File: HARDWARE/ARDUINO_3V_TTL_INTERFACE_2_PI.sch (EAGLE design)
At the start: 41 parts, among them J1 RASPBERRYPI-40-PIN-GPIO_SMT, Q1 BCM857BS, Q2 DMG2305UX, U1 ATMEGA328P, Y1 8MHz

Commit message: checkiong migration to new profile
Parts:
- D1: value GREEN -> RED
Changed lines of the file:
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@@
 <grid distance="0.1" unitdist="inch" unit="inch" style="lines" multiple="1" display="no" altdistance="0.01" altunitdist="inch" altunit="inch"/>
 <layers>
-<layer number="1" name="Top" color="4" fill="1" visible="yes" active="no"/>
-<layer number="2" name="Route2" color="16" fill="1" visible="yes" active="no"/>
-<layer number="3" name="Route3" color="17" fill="1" visible="yes" active="no"/>
-<layer number="4" name="Route4" color="18" fill="1" visible="yes" active="no"/>
-<layer number="5" name="Route5" color="19" fill="1" visible="yes" active="no"/>
-<layer number="6" name="Route6" color="25" fill="1" visible="yes" active="no"/>
-<layer number="7" name="Route7" color="26" fill="1" visible="yes" active="no"/>
-<layer number="8" name="Route8" color="27" fill="1" visible="yes" active="no"/>
-<layer number="9" name="Route9" color="28" fill="1" visible="yes" active="no"/>
-<layer number="10" name="Route10" color="29" fill="1" visible="yes" active="no"/>
-<layer number="11" name="Route11" color="30" fill="1" visible="yes" active="no"/>
-<layer number="12" name="Route12" color="20" fill="1" visible="yes" active="no"/>
-<layer number="13" name="Route13" color="21" fill="1" visible="yes" active="no"/>
-<layer number="14" name="Route14" color="22" fill="1" visible="yes" active="no"/>
-<layer number="15" name="Route15" color="23" fill="1" visible="yes" active="no"/>
-<layer number="16" name="Bottom" color="1" fill="1" visible="yes" active="no"/>
-<layer number="17" name="Pads" color="2" fill="1" visible="yes" active="no"/>
-<layer number="18" name="Vias" color="2" fill="1" visible="yes" active="no"/>
-<layer number="19" name="Unrouted" color="6" fill="1" visible="yes" active="no"/>
-<layer number="20" name="Dimension" color="24" fill="1" visible="yes" active="no"/>
-<layer number="21" name="tPlace" color="7" fill="1" visible="yes" active="no"/>
-<layer number="22" name="bPlace" color="7" fill="1" visible="yes" active="no"/>
-<layer number="23" name="tOrigins" color="15" fill="1" visible="yes" active="no"/>
-<layer number="24" name="bOrigins" color="15" fill="1" visible="yes" active="no"/>
-<layer number="25" name="tNames" color="7" fill="1" visible="yes" active="no"/>
-<layer number="26" name="bNames" color="7" fill="1" visible="yes" active="no"/>
-<layer number="27" name="tValues" color="7" fill="1" visible="yes" active="no"/>
-<layer number="28" name="bValues" color="7" fill="1" visible="yes" active="no"/>
+<layer number="1" name="Top" color="4" fill="1" visible="no" active="no"/>
+<layer number="2" name="Route2" color="16" fill="1" visible="no" active="no"/>
+<layer number="3" name="Route3" color="17" fill="1" visible="no" active="no"/>
+<layer number="4" name="Route4" color="18" fill="1" visible="no" active="no"/>
+<layer number="5" name="Route5" color="19" fill="1" visible="no" active="no"/>
+<layer number="6" name="Route6" color="25" fill="1" visible="no" active="no"/>
+<layer number="7" name="Route7" color="26" fill="1" visible="no" active="no"/>
+<layer number="8" name="Route8" color="27" fill="1" visible="no" active="no"/>
+<layer number="9" name="Route9" color="28" fill="1" visible="no" active="no"/>
+<layer number="10" name="Route10" color="29" fill="1" visible="no" active="no"/>
+<layer number="11" name="Route11" color="30" fill="1" visible="no" active="no"/>
+<layer number="12" name="Route12" color="20" fill="1" visible="no" active="no"/>
+<layer number="13" name="Route13" color="21" fill="1" visible="no" active="no"/>
+<layer number="14" name="Route14" color="22" fill="1" visible="no" active="no"/>
+<layer number="15" name="Route15" color="23" fill="1" visible="no" active="no"/>
+<layer number="16" name="Bottom" color="1" fill="1" visible="no" active="no"/>
+<layer number="17" name="Pads" color="2" fill="1" visible="no" active="no"/>
+<layer number="18" name="Vias" color="2" fill="1" visible="no" active="no"/>
+<layer number="19" name="Unrouted" color="6" fill="1" visible="no" active="no"/>
+<layer number="20" name="Dimension" color="24" fill="1" visible="no" active="no"/>
+<layer number="21" name="tPlace" color="7" fill="1" visible="no" active="no"/>
+<layer number="22" name="bPlace" color="7" fill="1" visible="no" active="no"/>
+<layer number="23" name="tOrigins" color="15" fill="1" visible="no" active="no"/>
+<layer number="24" name="bOrigins" color="15" fill="1" visible="no" active="no"/>
+<layer number="25" name="tNames" color="7" fill="1" visible="no" active="no"/>
+<layer number="26" name="bNames" color="7" fill="1" visible="no" active="no"/>
+<layer number="27" name="tValues" color="7" fill="1" visible="no" active="no"/>
+<layer number="28" name="bValues" color="7" fill="1" visible="no" active="no"/>
 <layer number="29" name="tStop" color="7" fill="3" visible="no" active="no"/>
 <layer number="30" name="bStop" color="7" fill="6" visible="no" active="no"/>
@@
 <layer number="35" name="tGlue" color="7" fill="4" visible="no" active="no"/>
 <layer number="36" name="bGlue" color="7" fill="5" visible="no" active="no"/>
-<layer number="37" name="tTest" color="7" fill="1" visible="yes" active="no"/>
-<layer number="38" name="bTest" color="7" fill="1" visible="yes" active="no"/>
+<layer number="37" name="tTest" color="7" fill="1" visible="no" active="no"/>
+<layer number="38" name="bTest" color="7" fill="1" visible="no" active="no"/>
 <layer number="39" name="tKeepout" color="4" fill="11" visible="no" active="no"/>
 <layer number="40" name="bKeepout" color="1" fill="11" visible="no" active="no"/>
@@
 <layer number="44" name="Drills" color="7" fill="1" visible="no" active="no"/>
 <layer number="45" name="Holes" color="7" fill="1" visible="no" active="no"/>
-<layer number="46" name="Milling" color="3" fill="1" visible="yes" active="no"/>
-<layer number="47" name="Measures" color="7" fill="1" visible="yes" active="no"/>
-<layer number="48" name="Document" color="7" fill="1" visible="yes" active="no"/>
-<layer number="49" name="Reference" color="7" fill="1" visible="yes" active="no"/>
-<layer number="50" name="dxf" color="7" fill="1" visible="yes" active="no"/>
-<layer number="51" name="tDocu" color="7" fill="1" visible="yes" active="no"/>
-<layer number="52" name="bDocu" color="7" fill="1" visible="yes" active="no"/>
-<layer number="53" name="tGND_GNDA" color="7" fill="9" visible="yes" active="no"/>
-<layer number="54" name="bGND_GNDA" color="1" fill="9" visible="yes" active="no"/>
-<layer number="56" name="wert" color="7" fill="1" visible="yes" active="no"/>
-<layer number="57" name="tCAD" color="7" fill="1" visible="yes" active="no"/>
-<layer number="59" name="tCarbon" color="7" fill="1" visible="yes" active="no"/>
-<layer number="60" name="bCarbon" color="7" fill="1" visible="yes" active="no"/>
+<layer number="46" name="Milling" color="3" fill="1" visible="no" active="no"/>
+<layer number="47" name="Measures" color="7" fill="1" visible="no" active="no"/>
+<layer number="48" name="Document" color="7" fill="1" visible="no" active="no"/>
+<layer number="49" name="Reference" color="7" fill="1" visible="no" active="no"/>
+<layer number="50" name="dxf" color="7" fill="1" visible="no" active="no"/>
+<layer number="51" name="tDocu" color="7" fill="1" visible="no" active="no"/>
+<layer number="52" name="bDocu" color="7" fill="1" visible="no" active="no"/>
+<layer number="53" name="tGND_GNDA" color="7" fill="9" visible="no" active="no"/>
+<layer number="54" name="bGND_GNDA" color="1" fill="9" visible="no" active="no"/>
+<layer number="56" name="wert" color="7" fill="1" visible="no" active="no"/>
+<layer number="57" name="tCAD" color="7" fill="1" visible="no" active="no"/>
+<layer number="59" name="tCarbon" color="7" fill="1" visible="no" active="no"/>
+<layer number="60" name="bCarbon" color="7" fill="1" visible="no" active="no"/>
 <layer number="88" name="SimResults" color="9" fill="1" visible="yes" active="yes"/>
 <layer number="89" name="SimProbes" color="9" fill="1" visible="yes" active="yes"/>
@@
 <part name="GND3" library="3-5-pin-smd" library_urn="urn:adsk.eagle:library:7170558" deviceset="GND" device=""/>
 <part name="C4" library="SparkFun-Capacitors" library_urn="urn:adsk.eagle:library:510" deviceset="0.1UF" device="-0603-100V-10%" package3d_urn="urn:adsk.eagle:package:37414/1" value="0.1uF"/>
-<part name="D1" library="SparkFun-LED" library_urn="urn:adsk.eagle:library:529" deviceset="LED-GREEN" device="0603" package3d_urn="urn:adsk.eagle:package:39354/1" value="GREEN"/>
+<part name="D1" library="SparkFun-LED" library_urn="urn:adsk.eagle:library:529" deviceset="LED-GREEN" device="0603" package3d_urn="urn:adsk.eagle:package:39354/1" value="RED"/>
 <part name="R2" library="SparkFun-Resistors" library_urn="urn:adsk.eagle:library:532" deviceset="10KOHM" device="-0603-1/10W-1%" package3d_urn="urn:adsk.eagle:package:39650/1" value="330"/>
 <part name="GND4" library="3-5-pin-smd" library_urn="urn:adsk.eagle:library:7170558" deviceset="GND" device=""/>

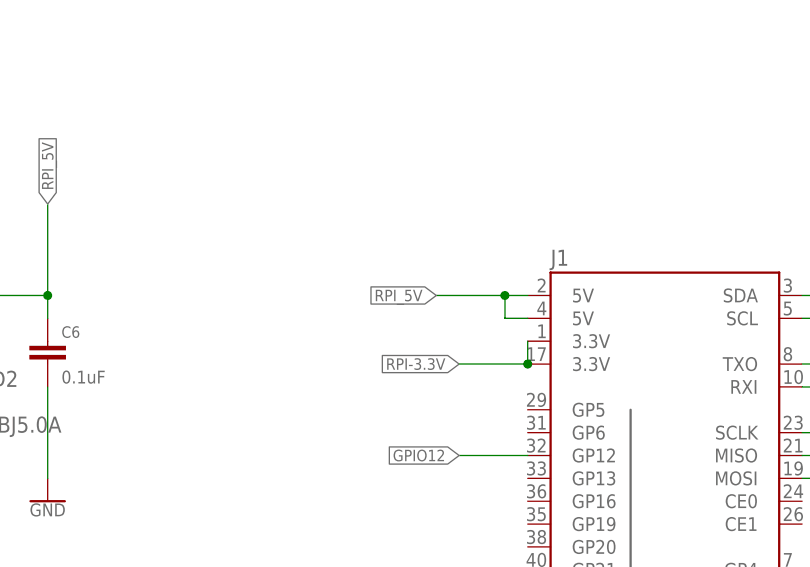
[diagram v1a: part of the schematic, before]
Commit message: added a jumper to separate ext voltage for testing it the volt reg citcuit doesn't work
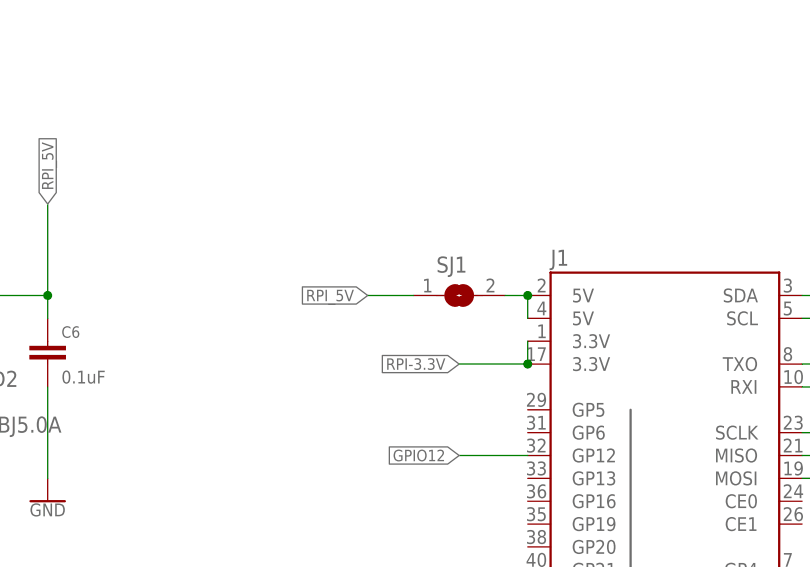
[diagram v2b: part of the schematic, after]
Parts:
- added SJ1: (no value), jumper:SJ
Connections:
- new net N$2: J1.5V@2, J1.5V@4, SJ1.2
- net RPI_5V: now also SJ1.1; no longer J1.5V@2, J1.5V@4
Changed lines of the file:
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@@
 <part name="GND5" library="3-5-pin-smd" library_urn="urn:adsk.eagle:library:7170558" deviceset="GND" device=""/>
 <part name="J13" library="SparkFun-Connectors" library_urn="urn:adsk.eagle:library:513" deviceset="CONN_09" device="" package3d_urn="urn:adsk.eagle:package:38153/1"/>
+<part name="SJ1" library="jumper" library_urn="urn:adsk.eagle:library:252" deviceset="SJ" device="" package3d_urn="urn:adsk.eagle:package:15471/1"/>
 </parts>
 <sheets>
@@
 <attribute name="VALUE" x="127" y="12.954" size="1.778" layer="96" font="vector"/>
 <attribute name="NAME" x="127" y="41.148" size="1.778" layer="95" font="vector"/>
+</instance>
+<instance part="SJ1" gate="1" x="45.72" y="68.58" smashed="yes">
+<attribute name="NAME" x="43.18" y="71.12" size="1.778" layer="95"/>
+<attribute name="VALUE" x="43.18" y="64.77" size="1.778" layer="96"/>
 </instance>
 </instances>
@@
 <net name="RPI_5V" class="0">
 <segment>
-<pinref part="J1" gate="G$1" pin="5V@2"/>
-<wire x1="53.34" y1="68.58" x2="50.8" y2="68.58" width="0.1524" layer="91"/>
-<wire x1="50.8" y1="68.58" x2="50.8" y2="66.04" width="0.1524" layer="91"/>
-<pinref part="J1" gate="G$1" pin="5V@4"/>
-<wire x1="50.8" y1="66.04" x2="53.34" y2="66.04" width="0.1524" layer="91"/>
-<junction x="50.8" y="68.58"/>
-<wire x1="43.18" y1="68.58" x2="50.8" y2="68.58" width="0.1524" layer="91"/>
-<label x="43.18" y="68.58" size="1.27" layer="95" font="fixed" rot="R180" xref="yes"/>
-</segment>
-<segment>
 <pinref part="Q2" gate="G$1" pin="S"/>
 <wire x1="-48.26" y1="91.44" x2="-48.26" y2="76.2" width="0.1524" layer="91"/>
@@
 <wire x1="137.16" y1="38.1" x2="142.24" y2="38.1" width="0.1524" layer="91"/>
 <label x="142.24" y="38.1" size="1.27" layer="95" font="fixed" xref="yes"/>
+</segment>
+<segment>
+<pinref part="SJ1" gate="1" pin="1"/>
+<wire x1="40.64" y1="68.58" x2="35.56" y2="68.58" width="0.1524" layer="91"/>
+<label x="35.56" y="68.58" size="1.27" layer="95" font="fixed" rot="R180" xref="yes"/>
 </segment>
 </net>
@@
 </segment>
 </net>
+<net name="N$2" class="0">
+<segment>
+<pinref part="J1" gate="G$1" pin="5V@4"/>
+<pinref part="J1" gate="G$1" pin="5V@2"/>
+<wire x1="53.34" y1="66.04" x2="53.34" y2="68.58" width="0.1524" layer="91"/>
+<pinref part="SJ1" gate="1" pin="2"/>
+<wire x1="50.8" y1="68.58" x2="53.34" y2="68.58" width="0.1524" layer="91"/>
+<junction x="53.34" y="68.58"/>
+</segment>
+</net>
